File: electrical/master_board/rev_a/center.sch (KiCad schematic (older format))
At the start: 15 parts, among them CN40 MIKROBUS_MATE;SMALL, CN41 MIKROBUS_MATE;MEDIUM, CN50 HCSR04;F1X4, CN51 HCSR04LP;F1X4, CN52 HCSR04LP;F1X4, CN53 HCSR04LP;F1X4, CN54 HCSR04;F1X4, CN55 HR2_EncoderMate;2XF1X3, CN56 HR2_EncoderMate;2XF1X3, CN57 RASPI;F2X20, CN58 ST_MATE;ST_MATE

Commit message: Added Pololu U3V70x Voltage Regulator to PCB's.
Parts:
- removed CN58: ST_MATE;ST_MATE, HR2:ST_MATE, symbol HR2:ST_MATE;ST_MATE
- added CN42: U3V70xMATE;F1x4+F1x5, HR2:U3V70xMATE_F1x4+F1x5, symbol HR2:U3V70xMATE;F1x4+F1x5
- added CN58: STADAPTER;F1x2+F1x4, HR2:STADAPTER_F1x2+F1x4, symbol HR2:STADAPTER;F1x2+F1x4
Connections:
- no-connect marks 111 -> 120
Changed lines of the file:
@@
 U 1 1 5F0D2FF0
 P 5300 2600
-F 0 "CN54" H 5650 2750 50  0000 C CNN
+F 0 "CN54" H 5600 2750 50  0000 C CNN
 F 1 "HCSR04;F1X4" H 5650 2150 50  0000 C CNN
 F 2 "HR2:HCSR04_F1x4" H 5500 2650 60  0001 L CNN
@@
 	1    0    0    -1
 $EndComp
-$Comp
-L HR2:ST_MATE;ST_MATE CN58
-U 1 1 5F14D9D8
-P 3300 3600
-F 0 "CN58" H 3650 3750 50  0000 C CNN
-F 1 "ST_MATE;ST_MATE" H 3650 2950 50  0000 C CNN
-F 2 "HR2:ST_MATE" H 3500 3650 60  0001 L CNN
-F 3 "ST Adaptor Mating Connector" H 3500 3450 60  0001 L CNN
-	1    3300 3600
-	1    0    0    -1
-$EndComp
-NoConn ~ 4000 3600
-NoConn ~ 4000 3700
-NoConn ~ 4000 3800
-NoConn ~ 4000 3900
-NoConn ~ 4000 4000
-NoConn ~ 4000 4100
+NoConn ~ 4200 3600
+NoConn ~ 4200 3700
+NoConn ~ 4200 3800
+NoConn ~ 4200 3900
+NoConn ~ 4200 4000
+NoConn ~ 4200 4100
 NoConn ~ 5300 1400
 $Comp
@@
 	-1   0    0    -1
 $EndComp
+$Comp
+L HR2:STADAPTER;F1x2+F1x4 CN58
+U 1 1 5F321197
+P 3500 3600
+F 0 "CN58" H 3800 3750 50  0000 C CNN
+F 1 "STADAPTER;F1x2+F1x4" H 3850 2950 50  0000 C CNN
+F 2 "HR2:STADAPTER_F1x2+F1x4" H 3700 3650 60  0001 L CNN
+F 3 "ST Adapter Mating Connectors" H 3700 3450 60  0001 L CNN
+F 4 "ST Adapter Mating Connectors" H 3700 3550 60  0001 L CNN "manf#"
+	1    3500 3600
+	1    0    0    -1
+$EndComp
+NoConn ~ 5050 4900
+NoConn ~ 5050 5000
+NoConn ~ 5050 5100
+NoConn ~ 5050 5200
+NoConn ~ 5050 5300
+NoConn ~ 5050 5400
+NoConn ~ 5050 5500
+NoConn ~ 5050 5600
+NoConn ~ 5050 5700
+$Comp
+L HR2:U3V70xMATE;F1x4+F1x5 CN42
+U 1 1 5F321F0B
+P 4250 4900
+F 0 "CN42" H 4550 5050 50  0000 C CNN
+F 1 "U3V70xMATE;F1x4+F1x5" H 4650 3950 50  0000 C CNN
+F 2 "HR2:U3V70xMATE_F1x4+F1x5" H 4450 4950 60  0001 L CNN
+F 3 "Pololu U3V70x Voltage Regulator Mating Connector" H 4450 4750 60  0001 L CNN
+F 4 "Pololu U3V70x Voltage Regulator Mating Connector" H 4450 4850 60  0001 L CNN "manf#"
+	1    4250 4900
+	1    0    0    -1
+$EndComp
 $EndSCHEMATC

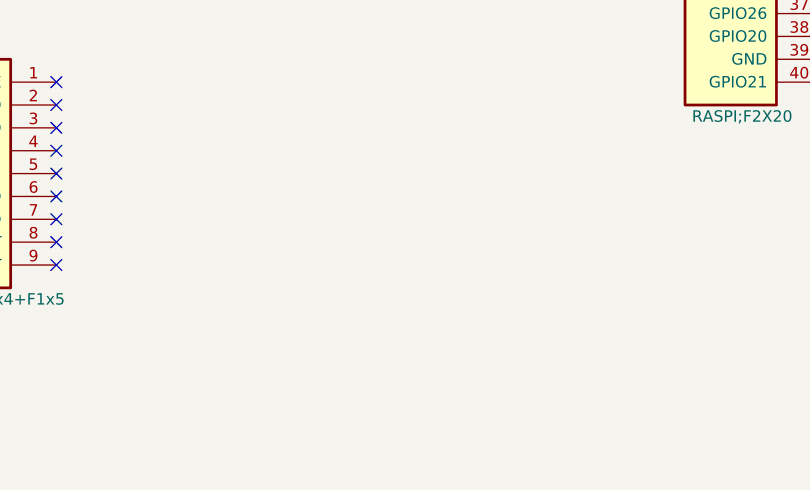
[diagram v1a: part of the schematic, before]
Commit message: Got the NUCLEO placed. Readjusted a few other parts.
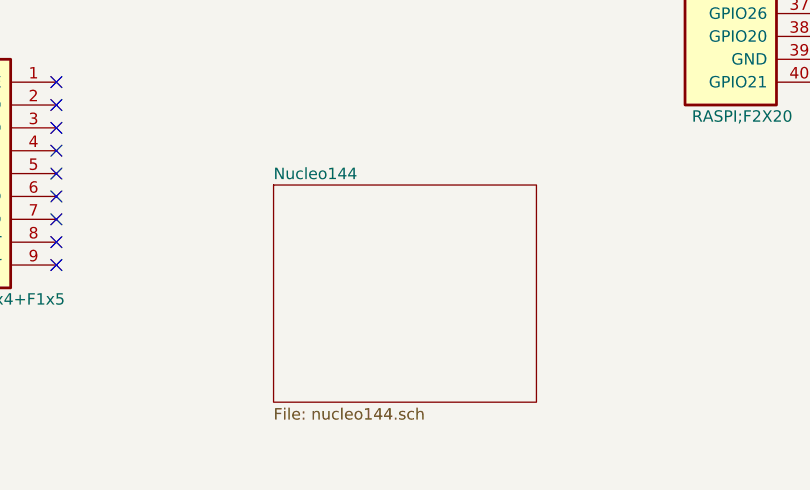
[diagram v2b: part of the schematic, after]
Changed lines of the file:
@@
 $Descr A 11000 8500
 encoding utf-8
-Sheet 1 1
+Sheet 1 2
 Title "HR2 Center PCB"
 Date "2020-06-13"
@@
 	1    0    0    -1
 $EndComp
+$Sheet
+S 6000 5350 1150 950
+U 5F3221A2
+F0 "Nucleo144" 50
+F1 "nucleo144.sch" 50
+$EndSheet
 $EndSCHEMATC

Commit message: Got Bridge connectors installed on PCB's. Tweaking still required.
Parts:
- added CN101: BRIDGE_NE_INNER;2xM1x1+M1x5, HR2:BRIDGE_NE_INNER_2xM1x1+M1x5, symbol HR2:BRIDGE_NE_INNER;2xM1x1+M1x5
- added CN102: BRIDGE_NW_INNER;M1x2+M2x5, HR2:BRIDGE_NW_INNER_M1x2+M2x5, symbol HR2:BRIDGE_NW_INNER;M1x2+M2x5
- added CN103: BRIDGE_SE_INNER;M1x8, HR2:BRIDGE_SE_INNER_M1x8, symbol HR2:BRIDGE_SE_INNER;M1x8
- added CN104: BRIDGE_SW_INNER;M1x8, HR2:BRIDGE_SW_INNER_M1x8, symbol HR2:BRIDGE_SW_INNER;M1x8
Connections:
- no-connect marks 120 -> 146
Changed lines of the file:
@@
 NoConn ~ 4200 4000
 NoConn ~ 4200 4100
-NoConn ~ 5300 1400
 $Comp
 L HR2:GROVE;20x20 GV5
@@
 F1 "nucleo144.sch" 50
 $EndSheet
+NoConn ~ 1800 1000
+NoConn ~ 1800 1450
+NoConn ~ 1800 1900
+NoConn ~ 1800 2000
+NoConn ~ 1800 2100
+NoConn ~ 1800 2200
+NoConn ~ 1800 2300
+$Comp
+L HR2:BRIDGE_NE_INNER;2xM1x1+M1x5 CN101
+U 1 1 5F385B77
+P 1100 1000
+F 0 "CN101" H 1450 1150 50  0000 C CNN
+F 1 "BRIDGE_NE_INNER;2xM1x1+M1x5" H 1450 850 50  0000 C CNN
+F 2 "HR2:BRIDGE_NE_INNER_2xM1x1+M1x5" H 1300 1050 60  0001 L CNN
+F 3 "" H 1300 850 60  0001 L CNN
+F 4 "NE Inner Bridge Connectors" H 1300 750 60  0001 L CNN "Field5"
+	1    1100 1000
+	1    0    0    -1
+$EndComp
+$Comp
+L HR2:BRIDGE_NE_INNER;2xM1x1+M1x5 CN101
+U 2 1 5F386C06
+P 1100 1450
+F 0 "CN101" H 1450 1600 50  0000 C CNN
+F 1 "BRIDGE_NE_INNER;2xM1x1+M1x5" H 1450 1300 50  0000 C CNN
+F 2 "HR2:BRIDGE_NE_INNER_2xM1x1+M1x5" H 1300 1500 60  0001 L CNN
+F 3 "" H 1300 1300 60  0001 L CNN
+F 4 "NE Inner Bridge Connectors" H 1300 1200 60  0001 L CNN "Field5"
+	2    1100 1450
+	1    0    0    -1
+$EndComp
+$Comp
+L HR2:BRIDGE_NE_INNER;2xM1x1+M1x5 CN101
+U 3 1 5F387693
+P 1100 1900
+F 0 "CN101" H 1450 2050 50  0000 C CNN
+F 1 "BRIDGE_NE_INNER;2xM1x1+M1x5" H 1450 1350 50  0000 C CNN
+F 2 "HR2:BRIDGE_NE_INNER_2xM1x1+M1x5" H 1300 1950 60  0001 L CNN
+F 3 "" H 1300 1750 60  0001 L CNN
+F 4 "NE Inner Bridge Connectors" H 1300 1650 60  0001 L CNN "Field5"
+	3    1100 1900
+	1    0    0    -1
+$EndComp
+$Comp
+L HR2:BRIDGE_NW_INNER;M1x2+M2x5 CN102
+U 1 1 5F386202
+P 2900 700
+F 0 "CN102" H 3250 850 50  0000 C CNN
+F 1 "BRIDGE_NW_INNER;M1x2+M2x5" H 3250 450 50  0000 C CNN
+F 2 "HR2:BRIDGE_NW_INNER_M1x2+M2x5" H 3100 750 60  0001 L CNN
+F 3 "" H 3100 550 60  0001 L CNN
+F 4 "NW Inner Bridge Connectors" H 3100 450 60  0001 L CNN "Field5"
+	1    2900 700
+	1    0    0    -1
+$EndComp
+$Comp
+L HR2:BRIDGE_NW_INNER;M1x2+M2x5 CN102
+U 2 1 5F3868C8
+P 2900 1200
+F 0 "CN102" H 3250 1350 50  0000 C CNN
+F 1 "BRIDGE_NW_INNER;M1x2+M2x5" H 3250 150 50  0000 C CNN
+F 2 "HR2:BRIDGE_NW_INNER_M1x2+M2x5" H 3100 1250 60  0001 L CNN
+F 3 "" H 3100 1050 60  0001 L CNN
+F 4 "NW Inner Bridge Connectors" H 3100 950 60  0001 L CNN "Field5"
+	2    2900 1200
+	1    0    0    -1
+$EndComp
+NoConn ~ 3600 700
+NoConn ~ 3600 800
+NoConn ~ 3600 1200
+NoConn ~ 3600 1300
+NoConn ~ 3600 1400
+NoConn ~ 3600 1500
+NoConn ~ 3600 1600
+NoConn ~ 3600 1700
+NoConn ~ 3600 1800
+NoConn ~ 3600 1900
+NoConn ~ 3600 2000
+NoConn ~ 3600 2100
+$Comp
+L HR2:BRIDGE_SE_INNER;M1x8 CN103
+U 1 1 5F386C55
+P 4150 900
+F 0 "CN103" H 4500 1050 50  0000 C CNN
+F 1 "BRIDGE_SE_INNER;M1x8" H 4500 50  50  0000 C CNN
+F 2 "HR2:BRIDGE_SE_INNER_M1x8" H 4350 950 60  0001 L CNN
+F 3 "" H 4350 750 60  0001 L CNN
+F 4 "SE Inner Bridge Connector" H 4350 650 60  0001 L CNN "Field5"
+	1    4150 900
+	1    0    0    -1
+$EndComp
+NoConn ~ 4850 900
+NoConn ~ 4850 1000
+NoConn ~ 4850 1100
+NoConn ~ 4850 1200
+NoConn ~ 4850 1300
+NoConn ~ 4850 1400
+NoConn ~ 4850 1500
+NoConn ~ 4850 1600
+$Comp
+L HR2:BRIDGE_SW_INNER;M1x8 CN104
+U 1 1 5F387577
+P 5350 900
+F 0 "CN104" H 5700 1050 50  0000 C CNN
+F 1 "BRIDGE_SW_INNER;M1x8" H 5700 50  50  0000 C CNN
+F 2 "HR2:BRIDGE_SW_INNER_M1x8" H 5550 950 60  0001 L CNN
+F 3 "" H 5550 750 60  0001 L CNN
+F 4 "SW Inner Bridge Connector" H 5550 650 60  0001 L CNN "Field5"
+	1    5350 900
+	1    0    0    -1
+$EndComp
 $EndSCHEMATC

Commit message: Started working on center board PCB.  Clean up stale schematics.
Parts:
- removed CN101: BRIDGE_NE_INNER;2xM1x1+M1x5, HR2:BRIDGE_NE_INNER_2xM1x1+M1x5, symbol HR2:BRIDGE_NE_INNER;2xM1x1+M1x5
- removed CN102: BRIDGE_NW_INNER;M1x2+M2x5, HR2:BRIDGE_NW_INNER_M1x2+M2x5, symbol HR2:BRIDGE_NW_INNER;M1x2+M2x5
- removed CN103: BRIDGE_SE_INNER;M1x8, HR2:BRIDGE_SE_INNER_M1x8, symbol HR2:BRIDGE_SE_INNER;M1x8
- removed CN104: BRIDGE_SW_INNER;M1x8, HR2:BRIDGE_SW_INNER_M1x8, symbol HR2:BRIDGE_SW_INNER;M1x8
- removed CN40: MIKROBUS_MATE;SMALL, HR2:MIKROBUS_SMALL_MATE, symbol HR2:MIKROBUS_MATE;SMALL
- removed CN41: MIKROBUS_MATE;MEDIUM, HR2:MIKROBUS_MEDIUM_MATE, symbol HR2:MIKROBUS_MATE;MEDIUM
- removed CN42: U3V70xMATE;F1x4+F1x5, HR2:U3V70xMATE_F1x4+F1x5, symbol HR2:U3V70xMATE;F1x4+F1x5
- removed CN50, CN54: HCSR04;F1X4, HR2:HCSR04_F1x4, symbol HR2:HCSR04;F1X4
- removed CN51, CN52, CN53: HCSR04LP;F1X4, HR2:HCSR04_F1x4LP, symbol HR2:HCSR04LP;F1X4
- removed CN55, CN56: HR2_EncoderMate;2XF1X3, HR2:ENCODER_MATE, symbol HR2:HR2_EncoderMate;2XF1X3
- removed CN57: RASPI;F2X20, HR2:RASPI_F2X20, symbol HR2:RASPI;F2X20
- removed CN58: STADAPTER;F1x2+F1x4, HR2:STADAPTER_F1x2+F1x4, symbol HR2:STADAPTER;F1x2+F1x4
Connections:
- wire segments 0 -> 3
- no-connect marks 146 -> 31
